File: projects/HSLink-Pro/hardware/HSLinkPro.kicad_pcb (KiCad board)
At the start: 4 copper layers, 26 x 35 mm, 126 parts, among them J1 IDC 2x10p 夹板, J2 USB_C_Receptacle_USB2.0, J3 Header 1.27 4P, Q1 AO3401A, Q2 2N7002, Q3 AO3401A, Q4 2N7002, SW1 1TS028A-1900-0600-CT, U1 HPM5301IEG1, U10 EA3036C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

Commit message: update: 更新原理图
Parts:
- removed C35: 0.1u, Capacitor_SMD:C_0402_1005Metric
- removed L3: 1.5u, Inductor_SMD:L_1008_2520Metric
- removed Q2, Q4: 2N7002, Package_TO_SOT_SMD:SOT-323_SC-70
- removed Q3: AO3401A, Package_TO_SOT_SMD:SOT-23
- removed R19, R20: 100k, Resistor_SMD:R_0402_1005Metric
- removed R29: 100R, Resistor_SMD:R_0402_1005Metric
- removed U7: SN74LVC1T45DCK, Package_TO_SOT_SMD:SOT-363_SC-70-6
- added C59: 1u, Capacitor_SMD:C_0402_1005Metric, F.Cu at (115.7, 59.2)
- added C60: 1u, Capacitor_SMD:C_0402_1005Metric, F.Cu at (111.7, 30.5)
- added C61: 1u, Capacitor_SMD:C_0402_1005Metric, F.Cu at (111.7, 33.3)
- added C62: 1u, Capacitor_SMD:C_0402_1005Metric, F.Cu at (95.3, 31.0)
- added C63: 1u, Capacitor_SMD:C_0402_1005Metric, F.Cu at (98.7, 29.0)
- added D2: 1N5819, Diode_SMD:D_SOD-523, F.Cu at (101.6, 59.9)
- added U19: ME6211C33U4G, Package_DFN_QFN:OnSemi_XDFN4-1EP_1.0x1.0mm_EP0.52x0.52mm, F.Cu at (99.6, 36.3)
- added U20: AW3512, Package_CSP:WLCSP-4-X1-WLB0909-4_0.89x0.89mm_P0.5mm, F.Cu at (113.8, 58.7)
- added U21: AW3512, Package_CSP:WLCSP-4-X1-WLB0909-4_0.89x0.89mm_P0.5mm, F.Cu at (113.8, 31.8)
- added U22: AW3512, Package_CSP:WLCSP-4-X1-WLB0909-4_0.89x0.89mm_P0.5mm, F.Cu at (96.8, 29.0)
- C40: value 1u -> 4.7u
- C41, C46: value 10u -> 22u
- C47: value 10u -> 0.1u; footprint Capacitor_SMD:C_0603_1608Metric -> Capacitor_SMD:C_0402_1005Metric
- C48: value 10u -> 1u
- C49: value 220p -> 1u
- C50: value 220p -> 6.8p
- C51: value 10u -> 1u; footprint Capacitor_SMD:C_0603_1608Metric -> Capacitor_SMD:C_0402_1005Metric
- L1: footprint Inductor_SMD:L_1008_2520Metric -> Inductor_SMD:L_Murata_DFE201610P
- L2: value 1.5u -> 2.2uH; footprint Inductor_SMD:L_1008_2520Metric -> Inductor_SMD:L_Murata_DFE201610P
- Q1: value AO3401A -> 2N7002; footprint Package_TO_SOT_SMD:SOT-23 -> Package_TO_SOT_SMD:SOT-323_SC-70
- R13: value 0R -> 1k; footprint Resistor_SMD:R_0603_1608Metric -> Resistor_SMD:R_0402_1005Metric
- R2: value 22.1k -> 100k
- U10: value EA3036C -> TLV62568DRL; footprint Package_DFN_QFN:QFN-20-1EP_3x3mm_P0.4mm_EP1.65x1.65mm -> Package_TO_SOT_SMD:SOT-563
- moved C51 35.0 mm to (111.5, 59.2), turned to 90 degrees
- moved C34 25.4 mm to (99.2, 33.3), turned to -90 degrees
- moved Q1 24.4 mm to (108.5, 36.6), turned to 0 degrees
- moved C53 21.8 mm to (101.8, 53.3), turned to 180 degrees
- moved C45 21.2 mm to (111.5, 57.4)
- moved C44 21.2 mm to (107.4, 57.4)
- moved C40 20.0 mm to (100.2, 33.3), turned to -90 degrees
- moved C47 9.25 mm to (95.3, 33.3), turned to 180 degrees
- moved R13 7.81 mm to (110.6, 36.2), turned to 90 degrees
- moved R2 7.41 mm to (94.8, 29.0), turned to -90 degrees
- moved R3 6.69 mm to (106.4, 36.2), turned to -90 degrees
- moved R21 2.68 mm to (113.8, 60.7), turned to 0 degrees
- moved C50 2.62 mm to (96.8, 31.4), turned to -90 degrees
- moved R4 2.62 mm to (97.7, 31.4), turned to -90 degrees
- moved R6 2.62 mm to (98.7, 31.4), turned to 90 degrees
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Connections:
- C34 pad 1: GND -> +5V
- C34 pad 2: +3V3 -> GND
- C41 pad 1: +5V -> TRANS_VCC
- C46 pad 1: +5V -> TRANS_VCC
- C47 pad 1: +5V -> TRANS_VCC
- C48 pad 1: GND -> +5V
- C48 pad 2: +3V3 -> GND
- C49 pad 1: Net-(U10A-FB1) -> +3V3
- C49 pad 2: +3V3 -> GND
- C51 pad 1: TRANS_VCC -> +5V
- C57 pad 1: +3V3 -> Net-(D1-VDD)
- D1 pad 1: +3V3 -> Net-(D1-VDD)
- L2 pad 1: +3V3 -> Net-(U10-SW)
- L2 pad 2: Net-(U10A-LX1) -> TRANS_VCC
- Q1 pad 1: Net-(Q1-G) -> /SRST
- Q1 pad 2: +5V -> GND
- Q1 pad 3: +5V_OUT -> /Interface /SRST
- R13 pad 2: VEE -> /Interface /SRST
- R2 pad 1: Net-(U10A-FB1) -> /PORT_EN
- R3 pad 1: Net-(U10A-FB1) -> /SRST
- R3 pad 2: +3V3 -> GND
- U1 pad 1: unconnected-(U1B-PA04/URT1.CTS/SPI0.CS0/TRGM0.P04/JTAG.TDO-Pad1) -> /PORT_EN
- U10 pad 1: GND -> /Power/TRANS_FB
- U10 pad 2: unconnected-(U10C-FB3-Pad2) -> GND
- U10 pad 3: /Power/TRANS_FB -> +5V
- U10 pad 4: GND -> Net-(U10-SW)
- U10 pad 5: GND -> +5V
- U10 pad 6: Net-(U10B-LX2) -> unconnected-(U10-NC-Pad6)
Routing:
- net +5V: track 96.5 -> 61.0 mm, vias 10 -> 8
- net /PORT_EN: track 0.00 -> 28.7 mm, vias 0 -> 2
- net Net-(D1-VDD): track 0.00 -> 27.8 mm, vias 0 -> 2
- net /Interface /SRST: track 4.43 -> 20.0 mm, vias 0 -> 2
- net Net-(U7-B): track 14.7 -> 0.00 mm, vias 2 -> 0
- net +3V3: track 154.4 -> 140.5 mm, vias 18 -> 16
- net VEE: track 77.8 -> 86.2 mm
- net Net-(Q1-G): track 6.42 -> 0.00 mm, vias 2 -> 0
- net Net-(Q3-G): track 5.25 -> 0.00 mm
- net TRANS_VCC_OUT: track 4.51 -> 8.23 mm
- net +5V_OUT: track 2.77 -> 6.33 mm
- net Net-(U10A-FB1): track 3.21 -> 0.00 mm
- net /Power/TRANS_VREF: track 28.2 -> 26.1 mm
- net Net-(U10B-LX2): track 2.14 -> 0.00 mm
- net GND: track 71.5 -> 73.6 mm, vias 64 -> 62
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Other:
- copper layers 4 -> 6
- board text added: "V1.1.0"

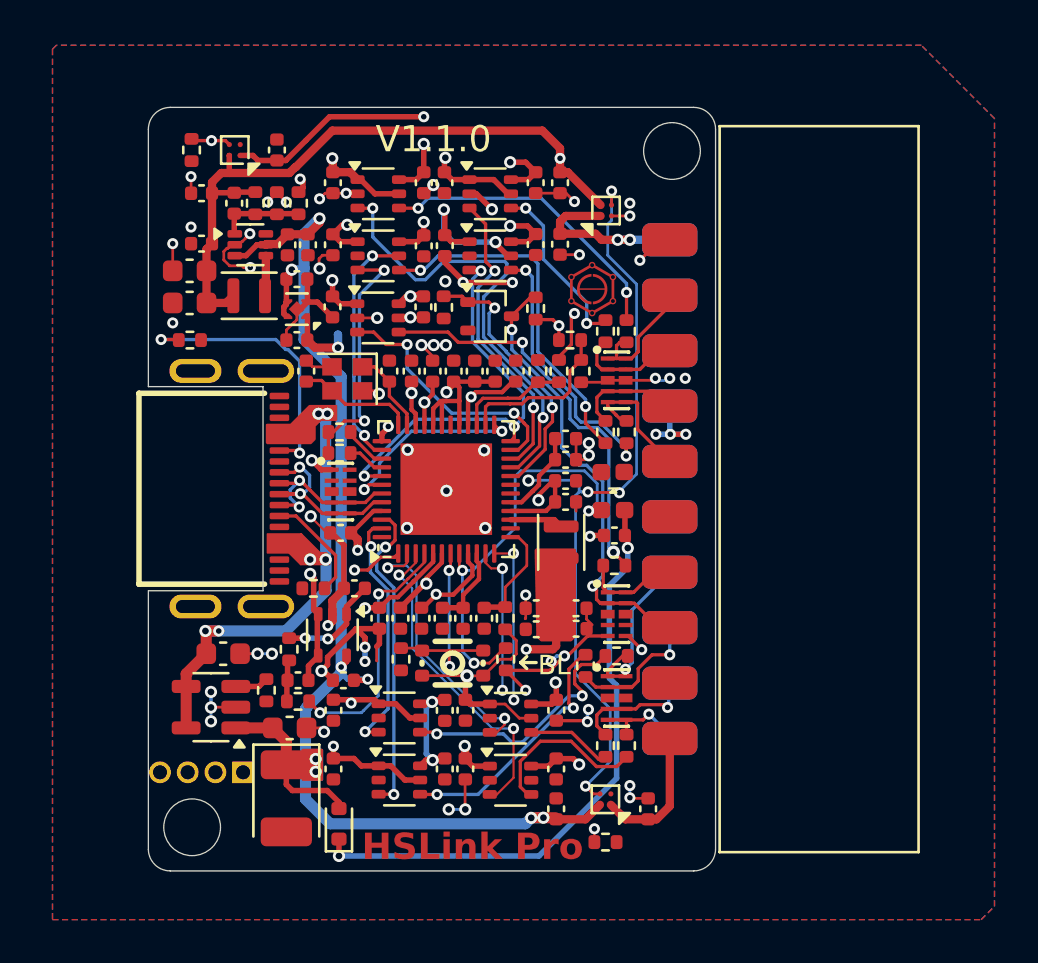
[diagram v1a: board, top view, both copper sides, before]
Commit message: update: 更新PCB
- 修改定位孔位置
- 修改Type-C位置
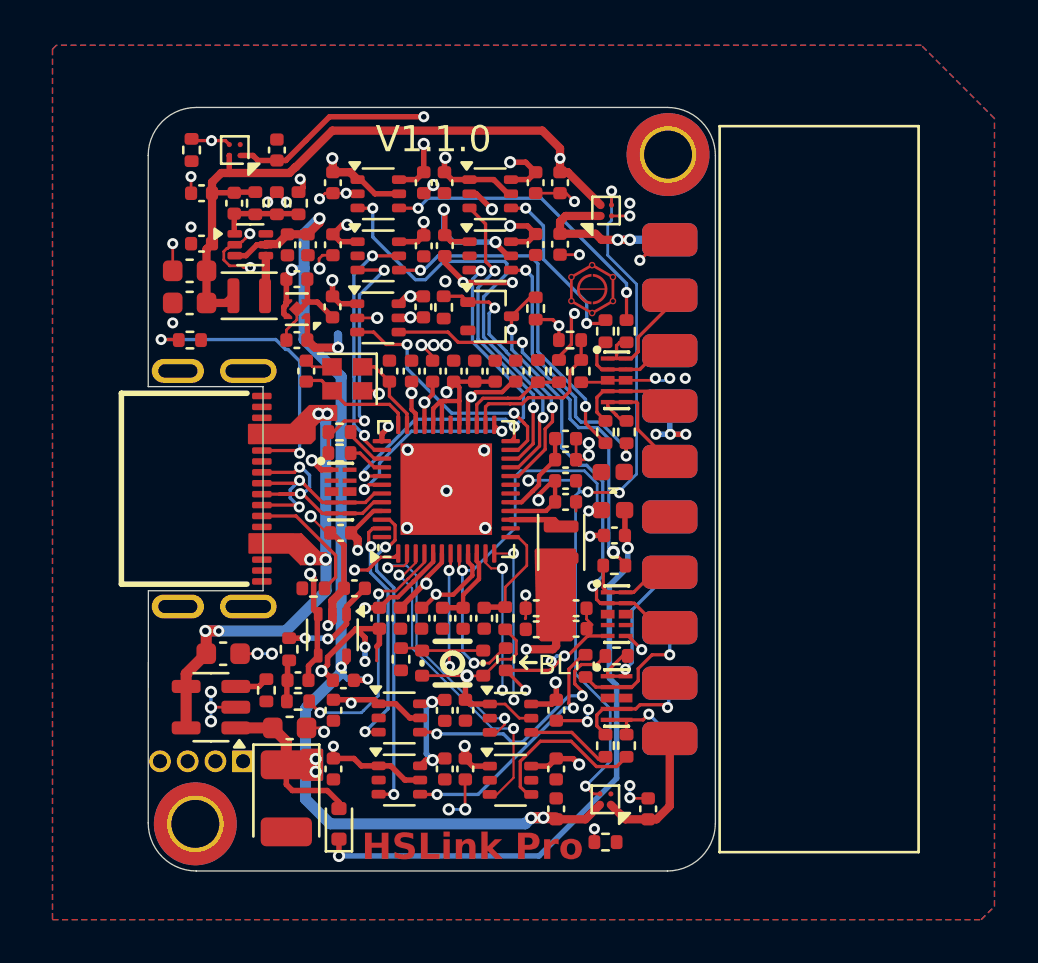
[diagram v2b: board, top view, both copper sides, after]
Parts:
- added REF**: MountingHole_2.2mm_M2_DIN965_Pad_TopBottom, MountingHole:MountingHole_2.2mm_M2_DIN965_Pad_TopBottom, F.Cu at (116.7, 29.2)
- added REF**: MountingHole_2.2mm_M2_DIN965_Pad_TopBottom, MountingHole:MountingHole_2.2mm_M2_DIN965_Pad_TopBottom, F.Cu at (95.0, 59.9)
- moved J2 0.80 mm to (96.1, 44.5)
- moved J3 0.50 mm to (97.2, 57.0)
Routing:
- net /USB_D-: track 7.50 -> 8.85 mm
- net /USB_D+: track 8.98 -> 10.3 mm
- net Net-(J2-CC1): track 12.8 -> 13.4 mm
- net Net-(J2-CC2): track 5.05 -> 5.72 mm
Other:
- outline, holes or cut-outs redrawn

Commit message: update: 添加RTT LOGO
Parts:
- added G***: LOGO, LOGO, B.Cu at (105.9, 29.5)

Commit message: update: 1.2.0硬件
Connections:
- D1 pad 4: /BOOT0 -> /WS2812
- U1 pad 46: /UART_RTS -> /WS2812
- U1 pad 48: unconnected-(U1B-PA05/TMR1.COMP2/URT1.DE/URT1.RTS/SPI0.SCLK/TRGM0.P05/JTAG.TDI-Pad48) -> /UART_RTS
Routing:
- net /WS2812: track 0.00 -> 16.9 mm, vias 0 -> 2
- net /BOOT0: track 18.6 -> 6.97 mm, vias 3 -> 2
- net /UART_RTS: track 14.2 -> 13.2 mm
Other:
- outline, holes or cut-outs redrawn
- board text added: "V1.2.0"
- board text removed: "V1.1.0"

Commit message: update: hardware 1.2.1
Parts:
- removed U20: AW3512, Package_CSP:WLCSP-4-X1-WLB0909-4_0.89x0.89mm_P0.5mm
- added U7: TPS22965, Package_SON:WSON-8-1EP_2x2mm_P0.5mm_EP0.9x1.6mm, F.Cu at (94.5, 30.0)
- U19: value ME6211C33U4G -> ME6211C33R5; footprint Package_DFN_QFN:OnSemi_XDFN4-1EP_1.0x1.0mm_EP0.52x0.52mm -> Package_TO_SOT_SMD:SOT-353_SC-70-5
- U21, U22: value AW3512 -> TPS22965; footprint Package_CSP:WLCSP-4-X1-WLB0909-4_0.89x0.89mm_P0.5mm -> Package_SON:WSON-8-1EP_2x2mm_P0.5mm_EP0.9x1.6mm
- moved U22 34.3 mm to (113.7, 58.8), turned to 0 degrees
- moved C48 3.47 mm to (97.6, 37.7), turned to 180 degrees
- moved C49 2.97 mm to (99.2, 34.7)
- moved R2 2.74 mm to (97.5, 29.5)
- moved C63 2.25 mm to (96.5, 29.5), turned to -90 degrees
- moved C60 1.75 mm to (112.7, 29.1), turned to 180 degrees
- moved C62 1.55 mm to (94.5, 32.3)
- moved C32 1.44 mm to (101.1, 34.7), turned to 180 degrees
- moved U21 1.43 mm to (112.7, 30.8), turned to 180 degrees
- moved C47 0.76 mm to (94.5, 33.3)
- moved U19 0.63 mm to (100.1, 36.7), turned to 0 degrees
- moved C34 0.23 mm to (99.0, 33.3)
- moved C41 0.23 mm to (94.5, 36.0)
- moved C46 0.23 mm to (94.5, 34.5)
- moved C50 0.23 mm to (96.5, 31.4)
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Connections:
- U19 pad 1: +3V3 -> +5V
- U19 pad 4: +5V -> unconnected-(U19-NC-Pad4)
- U19 pad 5: GND -> +3V3
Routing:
- net +5V: track 61.0 -> 69.9 mm, vias 8 -> 9
- net TRANS_VCC: track 40.0 -> 48.1 mm
- net VEE: track 86.2 -> 90.2 mm
- net /P_EN: track 46.6 -> 50.1 mm
- net Net-(J2-CC1): track 13.4 -> 10.8 mm
- net GND: track 73.6 -> 72.1 mm, vias 62 -> 70
- net /PORT_EN: track 28.7 -> 29.8 mm, vias 2 -> 3
- net +5V_OUT: track 6.33 -> 5.28 mm
- net +3V3: track 140.3 -> 141.2 mm
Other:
- copper layers 6 -> 4
- board text added: "V1.2.1"
- board text removed: "V1.2.0"
